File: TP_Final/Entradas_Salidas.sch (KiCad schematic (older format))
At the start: 89 parts, among them J109 BG 1x3, J110 BG2, J111 Conector pol. 1x3, J112 BG2, J113 Conector pol. 1x3, J114 Conector pol. 1x3, J115 BG2, J116 BG2, Q108 2N3904, Q109 2N3904, Q110 2N3904, U104 OP07, U105 OP07, U106 OP07, U107 LM7805_TO220, U108 LD3985M33R_TSOT23

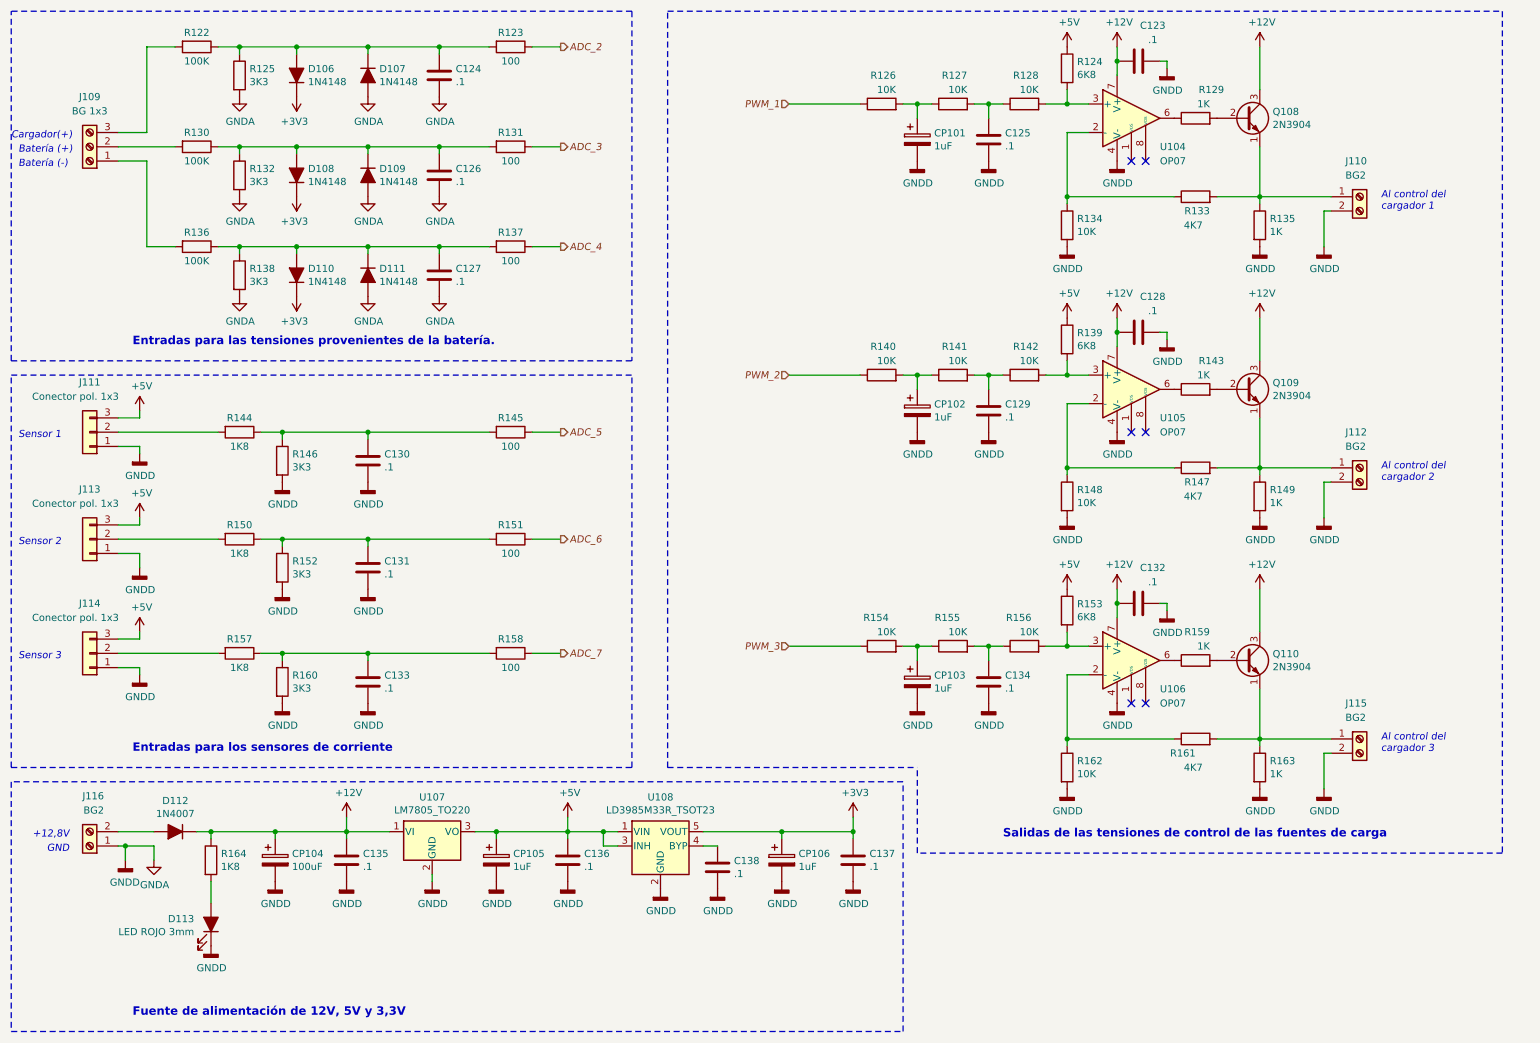
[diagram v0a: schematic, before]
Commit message: Se completa rotulo
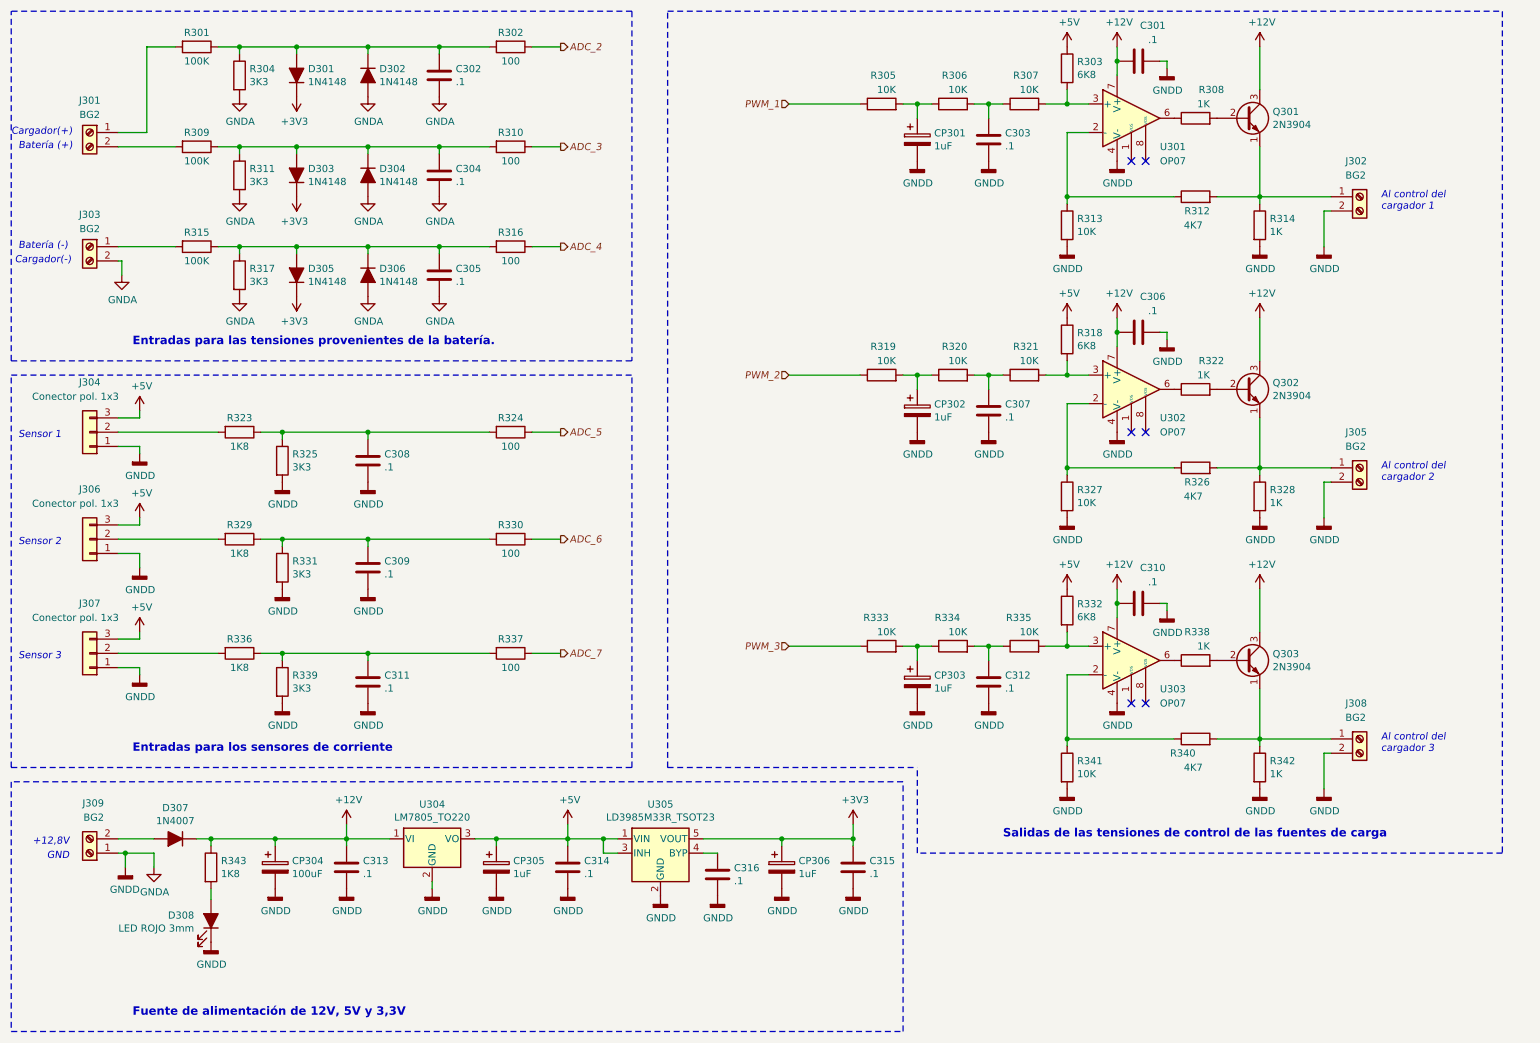
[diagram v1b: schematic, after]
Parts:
- removed J109: BG 1x3, TerminalBlock_Phoenix:TerminalBlock_Phoenix_PT-1,5-3-5.0-H_1x03_P5.00mm_Horizontal, symbol Connector:Screw_Terminal_01x03
- added J301, J303: BG2, TerminalBlock_Phoenix:TerminalBlock_Phoenix_PT-1,5-2-5.0-H_1x02_P5.00mm_Horizontal, symbol Connector:Screw_Terminal_01x02
- D307: renamed from D112; footprint Diode_THT:D_A-405_P7.62mm_Horizontal -> Diode_THT:D_DO-41_SOD81_P10.16mm_Horizontal
- renumbered C123 to C301, C124 to C302, C125 to C303, C126 to C304, C127 to C305, C128 to C306, C129 to C307, C130 to C308, C131 to C309, C132 to C310, C133 to C311, C134 to C312, C135 to C313, C136 to C314, C137 to C315, C138 to C316, CP101 to CP301, CP102 to CP302, CP103 to CP303, CP104 to CP304, CP105 to CP305, CP106 to CP306, D106 to D301, D107 to D302, D108 to D303, D109 to D304, D110 to D305, D111 to D306, D113 to D308, J110 to J302, J111 to J304, J112 to J305, J113 to J306, J114 to J307, J115 to J308, J116 to J309, Q108 to Q301, Q109 to Q302, Q110 to Q303, R122 to R301, R123 to R302, R124 to R303, R125 to R304, R126 to R305, R127 to R306, R128 to R307, R129 to R308, R130 to R309, R131 to R310, R132 to R311, R133 to R312, R134 to R313, R135 to R314, R136 to R315, R137 to R316, R138 to R317, R139 to R318, R140 to R319, R141 to R320, R142 to R321, R143 to R322, R144 to R323, R145 to R324, R146 to R325, R147 to R326, R148 to R327, R149 to R328, R150 to R329, R151 to R330, R152 to R331, R153 to R332, R154 to R333, R155 to R334, R156 to R335, R157 to R336, R158 to R337, R159 to R338, R160 to R339, R161 to R340, R162 to R341, R163 to R342, R164 to R343, U104 to U301, U105 to U302, U106 to U303, U107 to U304, U108 to U305
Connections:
- net GNDA: now also J303.2 (Pin_2)
- net at R301.2: now also J301.1 (Pin_1)
- net at R309.2: now also J301.2 (Pin_2)
- net at R315.2: now also J303.1 (Pin_1)
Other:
- note added: "Cargador(-)"
- moved on the sheet: C313, C314, C315, C316, CP304, CP305, CP306, D307, D308, J309, R343, U304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

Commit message: se agregan descripciones a componentes del esquemático
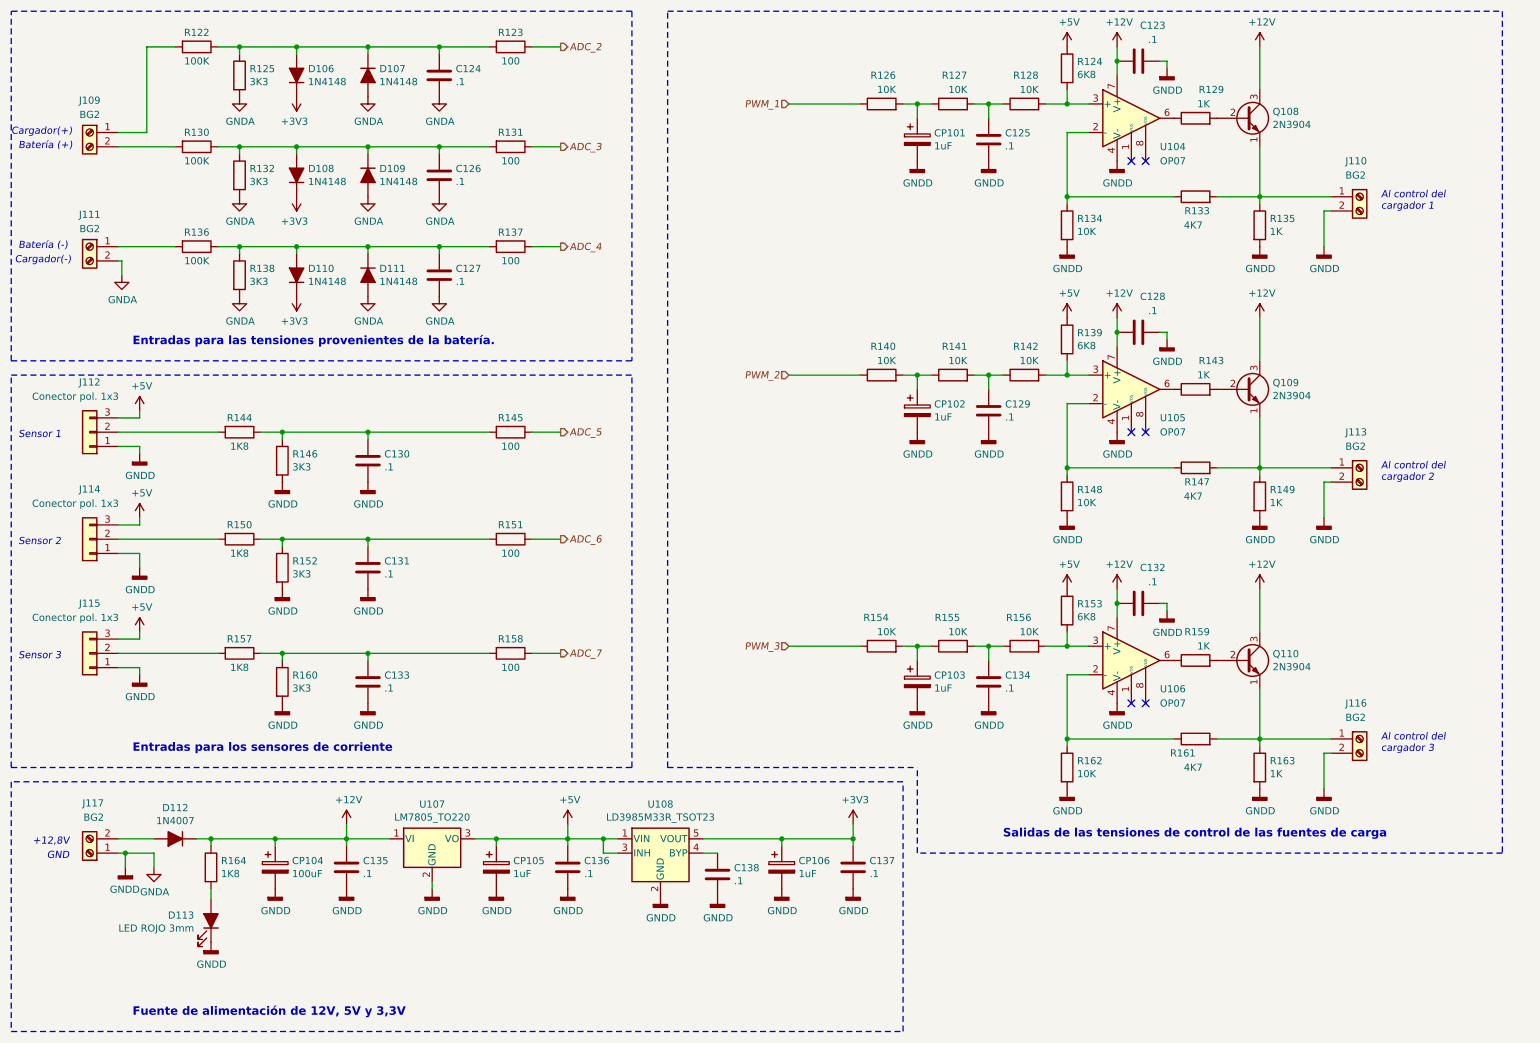
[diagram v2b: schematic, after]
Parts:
- removed J303: BG2, TerminalBlock_Phoenix:TerminalBlock_Phoenix_PT-1,5-2-5.0-H_1x02_P5.00mm_Horizontal, symbol Connector:Screw_Terminal_01x02
- removed J306, J307: Conector pol. 1x3, Connector_PinSocket_2.54mm:PinSocket_1x03_P2.54mm_Vertical, symbol Connector_Generic:Conn_01x03
- added J111: BG2, TerminalBlock_Phoenix:TerminalBlock_Phoenix_PT-1,5-2-5.0-H_1x02_P5.00mm_Horizontal, symbol Connector:Screw_Terminal_01x02
- added J114, J115: Conector pol. 1x3, Connector_PinHeader_2.54mm:PinHeader_1x03_P2.54mm_Vertical, symbol Connector_Generic:Conn_01x03
- J109: renamed from J301; Description (none) -> Bloque de terminales de tornillo PCB; Elemon part (none) -> BO5811874; Manufac. (none) -> XINYA
- J110: renamed from J302; Description (none) -> Bloque de terminales de tornillo PCB; Manufac. (none) -> XINYA
- J112: renamed from J304; footprint Connector_PinSocket_2.54mm:PinSocket_1x03_P2.54mm_Vertical -> Connector_PinHeader_2.54mm:PinHeader_1x03_P2.54mm_Vertical; Description (none) -> MA-03 VERT.3A P=2.5MM P/C.I; Manufac. (none) -> AUK Contractors
- J113: renamed from J305; Description (none) -> Bloque de terminales de tornillo PCB; Manufac. (none) -> XINYA
- J116: renamed from J308; Description (none) -> Bloque de terminales de tornillo PCB; Manufac. (none) -> XINYA
- J117: renamed from J309; Description (none) -> Bloque de terminales de tornillo PCB; Manufac. (none) -> XINYA
- U104: renamed from U301; Description (none) -> DIP-8 Ultralow Offset Voltage Operational Amplifier; Manufac. (none) -> Analog Device
- U105: renamed from U302; Description (none) -> DIP8 - Ultralow Offset VoltageOperational Amplifier; Manufac. (none) -> Analog Divice
- U106: renamed from U303; Description (none) -> DIP8 - Ultralow Offset Voltage Operational Amplifier; Manufac. (none) -> Analog Divice
- U107: renamed from U304; Description (none) -> 1A Fixed Voltage Regulator TO-220; Manufac. (none) -> On Semiconductor
- U108: renamed from U305; Description (none) -> Ultra low drop and low noise BiCMOS 3.3 voltage regulators; Manufac. (none) -> ST
- renumbered C301 to C123, C302 to C124, C303 to C125, C304 to C126, C305 to C127, C306 to C128, C307 to C129, C308 to C130, C309 to C131, C310 to C132, C311 to C133, C312 to C134, C313 to C135, C314 to C136, C315 to C137, C316 to C138, CP301 to CP101, CP302 to CP102, CP303 to CP103, CP304 to CP104, CP305 to CP105, CP306 to CP106, D301 to D106, D302 to D107, D303 to D108, D304 to D109, D305 to D110, D306 to D111, D307 to D112, D308 to D113, Q301 to Q108, Q302 to Q109, Q303 to Q110, R301 to R122, R302 to R123, R303 to R124, R304 to R125, R305 to R126, R306 to R127, R307 to R128, R308 to R129, R309 to R130, R310 to R131, R311 to R132, R312 to R133, R313 to R134, R314 to R135, R315 to R136, R316 to R137, R317 to R138, R318 to R139, R319 to R140, R320 to R141, R321 to R142, R322 to R143, R323 to R144, R324 to R145, R325 to R146, R326 to R147, R327 to R148, R328 to R149, R329 to R150, R330 to R151, R331 to R152, R332 to R153, R333 to R154, R334 to R155, R335 to R156, R336 to R157, R337 to R158, R338 to R159, R339 to R160, R340 to R161, R341 to R162, R342 to R163, R343 to R164
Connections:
- net +5V: now also J114.3 (Pin_3), J115.3 (Pin_3)
- net GNDA: now also J111.2 (Pin_2), J114.1 (Pin_1), J115.1 (Pin_1)
- net at R136.2: now also J111.1 (Pin_1)
- net at R150.2: now also J114.2 (Pin_2)
- net at R157.2: now also J115.2 (Pin_2)

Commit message: Se avanza con el ruteo del PCB
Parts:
- removed C138: .1, Capacitor_SMD:C_0805_2012Metric, symbol Device:C
- removed U108: LD3985M33R_TSOT23, Package_TO_SOT_SMD:TSOT-23-5, symbol Regulator_Linear:LD3985G33R_TSOT23
- added U108: LD1117S33TR_SOT223, Package_TO_SOT_SMD:SOT-223-3_TabPin2, symbol Regulator_Linear:LD1117S33TR_SOT223
- J112, J114, J115: footprint Connector_PinHeader_2.54mm:PinHeader_1x03_P2.54mm_Vertical -> Connector_JST:JST_EH_B3B-EH-A_1x03_P2.50mm_Vertical
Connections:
- net +3V3: now also U108.2 (VO)
- net +5V: now also U108.3 (VI)
- net GNDA: now also U108.1 (GND)
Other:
- note added: "Al control de tensión \nde la fuente 1"
- note added: "Al control de tensión \nde la fuente 2"
- note added: "Al control de tensión \nde la fuente 3"
- note removed: "Al control del \ncargador 1"
- note removed: "Al control del \ncargador 2"
- note removed: "Al control del \ncargador 3"
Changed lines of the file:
@@
 F 0 "J112" H 1200 3150 50  0000 C CNN
 F 1 "Conector pol. 1x3" H 1300 3250 50  0000 C CNN
-F 2 "Connector_PinHeader_2.54mm:PinHeader_1x03_P2.54mm_Vertical" H 1200 3500 50  0001 C CNN
+F 2 "Connector_JST:JST_EH_B3B-EH-A_1x03_P2.50mm_Vertical" H 1200 3500 50  0001 C CNN
 F 3 "http://www.aukconnector.com/object/AUKDrawing/VHXXD-XX-H.pdf" H 1200 3500 50  0001 C CNN
 F 4 "AUK Contractors" H 1200 3500 50  0001 C CNN "Manufac."
@@
 $EndComp
 $Comp
-L power:GNDD #PWR0234
+L power:GNDD #PWR0233
 U 1 1 60D2089A
 P 2050 7075
-F 0 "#PWR0234" H 2050 6825 50  0001 C CNN
+F 0 "#PWR0233" H 2050 6825 50  0001 C CNN
 F 1 "GNDD" H 2054 6920 50  0000 C CNN
 F 2 "" H 2050 7075 50  0001 C CNN
@@
 $EndComp
 $Comp
-L power:GNDD #PWR0230
+L power:GNDD #PWR0231
 U 1 1 60D7FDCF
 P 6050 6700
-F 0 "#PWR0230" H 6050 6450 50  0001 C CNN
+F 0 "#PWR0231" H 6050 6450 50  0001 C CNN
 F 1 "GNDD" H 6054 6545 50  0000 C CNN
 F 2 "" H 6050 6700 50  0001 C CNN
@@
 $EndComp
 $Comp
-L power:GNDD #PWR0231
+L power:GNDD #PWR0232
 U 1 1 60D7FDD9
 P 6550 6700
-F 0 "#PWR0231" H 6550 6450 50  0001 C CNN
+F 0 "#PWR0232" H 6550 6450 50  0001 C CNN
 F 1 "GNDD" H 6554 6545 50  0000 C CNN
 F 2 "" H 6550 6700 50  0001 C CNN
@@
 	3900 6350 4050 6350
 Wire Wire Line
-	4800 6350 4800 6450
-Wire Wire Line
-	4800 6450 4900 6450
-Connection ~ 4800 6350
-Wire Wire Line
-	4800 6350 4900 6350
-Wire Wire Line
 	4550 6400 4550 6350
 Connection ~ 4550 6350
 Wire Wire Line
-	4550 6350 4800 6350
-Wire Wire Line
 	4050 6400 4050 6350
 Connection ~ 4050 6350
@@
 Wire Wire Line
 	6050 6350 6550 6350
-Wire Wire Line
-	5500 6450 5600 6450
-$Comp
-L power:GNDD #PWR0233
-U 1 1 60D9167D
-P 5600 6750
-F 0 "#PWR0233" H 5600 6500 50  0001 C CNN
-F 1 "GNDD" H 5604 6595 50  0000 C CNN
-F 2 "" H 5600 6750 50  0001 C CNN
-F 3 "" H 5600 6750 50  0001 C CNN
-	1    5600 6750
-	1    0    0    -1
-$EndComp
-$Comp
-L Device:C C138
-U 1 1 60D91677
-P 5600 6600
-F 0 "C138" H 5715 6646 50  0000 L CNN
-F 1 ".1" H 5715 6555 50  0000 L CNN
-F 2 "Capacitor_SMD:C_0805_2012Metric" H 5638 6450 50  0001 C CNN
-F 3 "~" H 5600 6600 50  0001 C CNN
-	1    5600 6600
-	1    0    0    -1
-$EndComp
-$Comp
-L Regulator_Linear:LD3985G33R_TSOT23 U108
-U 1 1 60D8B68E
-P 5200 6450
-F 0 "U108" H 5200 6792 50  0000 C CNN
-F 1 "LD3985M33R_TSOT23" H 5200 6701 50  0000 C CNN
-F 2 "Package_TO_SOT_SMD:TSOT-23-5" H 5200 6775 50  0001 C CIN
-F 3 "http://www.st.com/internet/com/TECHNICAL_RESOURCES/TECHNICAL_LITERATURE/DATASHEET/CD00003395.pdf" H 5200 6500 50  0001 C CNN
-F 4 "ST" H 5200 6450 50  0001 C CNN "Manufac."
-F 5 "Ultra low drop and low noise BiCMOS 3.3 voltage regulators" H 5200 6450 50  0001 C CNN "Description"
-F 6 "497-3504-1-ND" H 5200 6450 50  0001 C CNN "Difikey part"
-	1    5200 6450
-	1    0    0    -1
-$EndComp
-$Comp
-L power:GNDD #PWR0232
+$Comp
+L power:GNDD #PWR0230
 U 1 1 60E6D511
-P 5200 6750
-F 0 "#PWR0232" H 5200 6500 50  0001 C CNN
-F 1 "GNDD" H 5204 6595 50  0000 C CNN
-F 2 "" H 5200 6750 50  0001 C CNN
-F 3 "" H 5200 6750 50  0001 C CNN
-	1    5200 6750
+P 5200 6700
+F 0 "#PWR0230" H 5200 6450 50  0001 C CNN
+F 1 "GNDD" H 5204 6545 50  0000 C CNN
+F 2 "" H 5200 6700 50  0001 C CNN
+F 3 "" H 5200 6700 50  0001 C CNN
+	1    5200 6700
 	1    0    0    -1
 $EndComp
@@
 Text Notes 900  6500 0    50   Italic 0
 GND
-Text Notes 10250 1950 0    50   Italic 0
-Al control del \ncargador 1
 Text Notes 10250 3850 0    50   Italic 0
-Al control del \ncargador 2
+Al control de tensión \nde la fuente 2
 Text Notes 10250 5750 0    50   Italic 0
-Al control del \ncargador 3
+Al control de tensión \nde la fuente 3
 Wire Notes Line
 	5250 5850 7000 5850
@@
 F 0 "J114" H 1200 3900 50  0000 C CNN
 F 1 "Conector pol. 1x3" H 1300 4000 50  0000 C CNN
-F 2 "Connector_PinHeader_2.54mm:PinHeader_1x03_P2.54mm_Vertical" H 1200 4250 50  0001 C CNN
+F 2 "Connector_JST:JST_EH_B3B-EH-A_1x03_P2.50mm_Vertical" H 1200 4250 50  0001 C CNN
 F 3 "http://www.aukconnector.com/object/AUKDrawing/VHXXD-XX-H.pdf" H 1200 4250 50  0001 C CNN
 F 4 "AUK Contractors" H 1200 4250 50  0001 C CNN "Manufac."
@@
 F 0 "J115" H 1200 4700 50  0000 C CNN
 F 1 "Conector pol. 1x3" H 1300 4800 50  0000 C CNN
-F 2 "Connector_PinHeader_2.54mm:PinHeader_1x03_P2.54mm_Vertical" H 1200 5050 50  0001 C CNN
+F 2 "Connector_JST:JST_EH_B3B-EH-A_1x03_P2.50mm_Vertical" H 1200 5050 50  0001 C CNN
 F 3 "http://www.aukconnector.com/object/AUKDrawing/VHXXD-XX-H.pdf" H 1200 5050 50  0001 C CNN
 F 4 "AUK Contractors" H 1200 5050 50  0001 C CNN "Manufac."
@@
 	1    0    0    -1
 $EndComp
+Text Notes 10250 1950 0    50   Italic 0
+Al control de tensión \nde la fuente 1
+$Comp
+L Regulator_Linear:LD1117S33TR_SOT223 U108
+U 1 1 60979DB7
+P 5200 6350
+F 0 "U108" H 5200 6592 50  0000 C CNN
+F 1 "LD1117S33TR_SOT223" H 5200 6501 50  0000 C CNN
+F 2 "Package_TO_SOT_SMD:SOT-223-3_TabPin2" H 5200 6550 50  0001 C CNN
+F 3 "http://www.st.com/st-web-ui/static/active/en/resource/technical/document/datasheet/CD00000544.pdf" H 5300 6100 50  0001 C CNN
+F 4 "ST" H 5200 6350 50  0001 C CNN "Manufac."
+F 5 "Fixed low drop positive voltage regulator" H 5200 6350 50  0001 C CNN "Description"
+F 6 "497-1242-1-ND" H 5200 6350 50  0001 C CNN "Digikey part"
+	1    5200 6350
+	1    0    0    -1
+$EndComp
+Wire Wire Line
+	5200 6700 5200 6650
+Wire Wire Line
+	4550 6350 4900 6350
 $EndSCHEMATC
